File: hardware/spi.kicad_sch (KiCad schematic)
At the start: 20 parts, among them J2 Conn_LAN_Module, J3 Conn_SD_Module, J4 Conn_SD_ACT_LED, U2 DG412, U3 74LVC00, U5 74LVC32, U6 74LVC74, U7 74LVC02

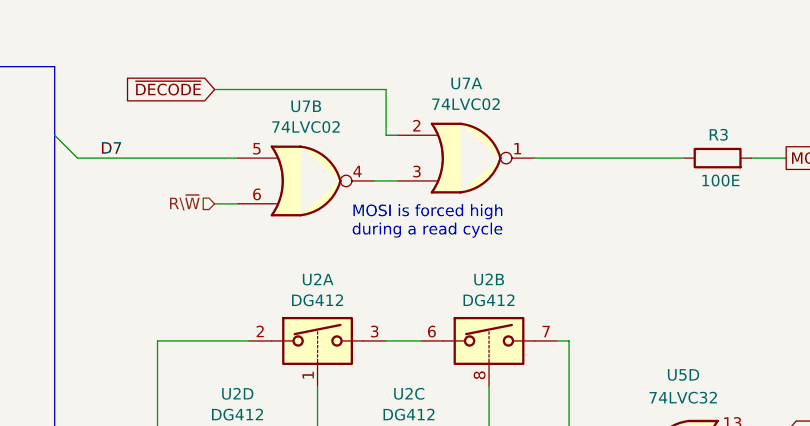
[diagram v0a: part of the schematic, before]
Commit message: Added info on MOSI setup mod to schematics
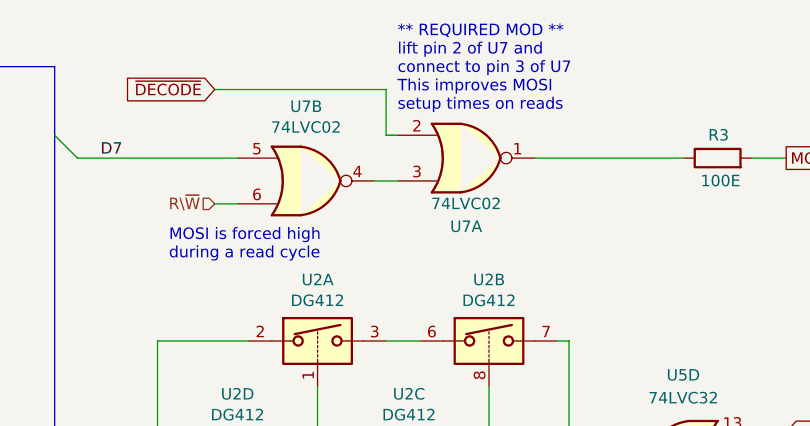
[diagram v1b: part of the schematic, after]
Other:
- note added: "** REQUIRED MOD ** lift pin 2 of U7 and connect to pin 3 of U7 This improves MOSI setup times on reads"
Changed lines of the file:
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@@
     (comment 1 "rev 1.1: new address decoder, 3V3 supplied by SD module, MOSI forced high on read")
     (comment 2 "rev 1.2: fixed small but fatal bug in address decoder, smaller PCB to clear shield")
+    (comment 3 "NOTE 5-12-2022: mod required on U7, see schematics")
   )
   (junction (at 78.74 153.67) (diameter 0) (color 0 0 0 0)
@@
     (effects (font (size 1.27 1.27)) (justify left bottom))
   )
-  (text "MOSI is forced high\nduring a read cycle" (at 168.91 36.83 0)
+  (text "MOSI is forced high\nduring a read cycle" (at 148.59 39.37 0)
     (effects (font (size 1.27 1.27)) (justify left bottom))
   )
@@
     (effects (font (size 1.27 1.27)) (justify left bottom))
   )
+  (text "** REQUIRED MOD **\nlift pin 2 of U7 and \nconnect to pin 3 of U7\nThis improves MOSI \nsetup times on reads"
+    (at 173.99 22.86 0)
+    (effects (font (size 1.27 1.27)) (justify left bottom))
+  )
   (label "D8" (at 140.97 95.25 0)
     (effects (font (size 1.27 1.27)) (justify left bottom))
@@
   (symbol (lib_id "74xx:74HC02") (at 181.61 27.94 0) (unit 1)
     (in_bom yes) (on_board yes)
-    (property "Reference" "U7" (id 0) (at 181.61 19.685 0))
-    (property "Value" "74LVC02" (id 1) (at 181.61 21.9964 0))
+    (property "Reference" "U7" (id 0) (at 181.61 35.56 0))
+    (property "Value" "74LVC02" (id 1) (at 181.61 33.02 0))
     (property "Footprint" "Package_SO:SOIC-14_3.9x8.7mm_P1.27mm" (id 2) (at 181.61 27.94 0)
       (effects (font (size 1.27 1.27)) hide)

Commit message: New Revision 1.3 which improves MOSI setup times on reads
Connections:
- net GND: now also U7.2
- net ~{DECODE}: no longer U7.2
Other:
- note removed: "** REQUIRED MOD ** lift pin 2 of U7 and connect to pin 3 of U7 This improves MOSI setup times on reads"
- moved on the sheet: R3, U7A, U7B
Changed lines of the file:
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@@
   (title_block
     (title "A500 simple SPI controller")
-    (date "2022-11-16")
-    (rev "1.2")
+    (date "2022-12-05")
+    (rev "1.3")
     (company "Dennis van Weeren")
     (comment 1 "rev 1.1: new address decoder, 3V3 supplied by SD module, MOSI forced high on read")
     (comment 2 "rev 1.2: fixed small but fatal bug in address decoder, smaller PCB to clear shield")
-    (comment 3 "NOTE 5-12-2022: mod required on U7, see schematics")
+    (comment 3 "rev 1.3: improved MOSI setup time on reads")
   )
   (junction (at 78.74 153.67) (diameter 0) (color 0 0 0 0)
@@
     (stroke (width 0) (type default) (color 0 0 0 0))
   )
-  (bus_entry (at 135.89 25.4) (size 2.54 2.54)
+  (bus_entry (at 135.89 21.59) (size 2.54 2.54)
     (stroke (width 0) (type default) (color 0 0 0 0))
   )
@@
     (stroke (width 0) (type default) (color 0 0 0 0))
   )
+  (wire (pts (xy 176.53 31.75) (xy 176.53 33.02))
+    (stroke (width 0) (type default) (color 0 0 0 0))
+  )
   (wire (pts (xy 15.24 153.67) (xy 27.94 153.67))
     (stroke (width 0) (type default) (color 0 0 0 0))
@@
     (stroke (width 0) (type default) (color 0 0 0 0))
   )
+  (wire (pts (xy 177.8 31.75) (xy 176.53 31.75))
+    (stroke (width 0) (type default) (color 0 0 0 0))
+  )
   (wire (pts (xy 214.63 63.5) (xy 214.63 64.77))
     (stroke (width 0) (type default) (color 0 0 0 0))
@@
     (stroke (width 0) (type default) (color 0 0 0 0))
   )
-  (wire (pts (xy 173.99 25.4) (xy 172.72 25.4))
-    (stroke (width 0) (type default) (color 0 0 0 0))
-  )
   (wire (pts (xy 203.2 100.33) (xy 203.2 104.14))
     (stroke (width 0) (type default) (color 0 0 0 0))
@@
     (stroke (width 0) (type default) (color 0 0 0 0))
   )
-  (wire (pts (xy 171.45 30.48) (xy 173.99 30.48))
+  (wire (pts (xy 171.45 26.67) (xy 177.8 26.67))
     (stroke (width 0) (type default) (color 0 0 0 0))
   )
@@
     (stroke (width 0) (type default) (color 0 0 0 0))
   )
-  (wire (pts (xy 138.43 27.94) (xy 156.21 27.94))
+  (wire (pts (xy 138.43 24.13) (xy 156.21 24.13))
     (stroke (width 0) (type default) (color 0 0 0 0))
   )
@@
     (stroke (width 0) (type default) (color 0 0 0 0))
   )
-  (wire (pts (xy 153.67 20.32) (xy 172.72 20.32))
-    (stroke (width 0) (type default) (color 0 0 0 0))
-  )
   (bus (pts (xy 34.29 58.42) (xy 34.29 76.2))
     (stroke (width 0) (type default) (color 0 0 0 0))
@@
     (stroke (width 0) (type default) (color 0 0 0 0))
   )
-  (wire (pts (xy 172.72 25.4) (xy 172.72 20.32))
-    (stroke (width 0) (type default) (color 0 0 0 0))
-  )
   (wire (pts (xy 15.24 152.4) (xy 15.24 153.67))
     (stroke (width 0) (type default) (color 0 0 0 0))
@@
     (stroke (width 0) (type default) (color 0 0 0 0))
   )
-  (wire (pts (xy 189.23 27.94) (xy 205.74 27.94))
+  (wire (pts (xy 193.04 29.21) (xy 205.74 29.21))
     (stroke (width 0) (type default) (color 0 0 0 0))
   )
@@
     (stroke (width 0) (type default) (color 0 0 0 0))
   )
-  (wire (pts (xy 213.36 27.94) (xy 217.17 27.94))
+  (wire (pts (xy 213.36 29.21) (xy 217.17 29.21))
     (stroke (width 0) (type default) (color 0 0 0 0))
   )
@@
     (stroke (width 0) (type default) (color 0 0 0 0))
   )
-  (bus (pts (xy 135.89 25.4) (xy 135.89 58.42))
+  (bus (pts (xy 135.89 21.59) (xy 135.89 58.42))
     (stroke (width 0) (type default) (color 0 0 0 0))
   )
@@
     (stroke (width 0) (type default) (color 0 0 0 0))
   )
-  (bus (pts (xy 135.89 17.78) (xy 135.89 25.4))
+  (bus (pts (xy 135.89 17.78) (xy 135.89 21.59))
     (stroke (width 0) (type default) (color 0 0 0 0))
   )
@@
     (stroke (width 0) (type default) (color 0 0 0 0))
   )
-  (wire (pts (xy 156.21 33.02) (xy 153.67 33.02))
+  (wire (pts (xy 156.21 29.21) (xy 153.67 29.21))
     (stroke (width 0) (type default) (color 0 0 0 0))
   )
@@
     (effects (font (size 1.27 1.27)) (justify left bottom))
   )
-  (text "MOSI is forced high\nduring a read cycle" (at 148.59 39.37 0)
+  (text "MOSI is forced high\nduring a read cycle" (at 148.59 35.56 0)
     (effects (font (size 1.27 1.27)) (justify left bottom))
   )
@@
     (effects (font (size 1.27 1.27)) (justify left bottom))
   )
-  (text "** REQUIRED MOD **\nlift pin 2 of U7 and \nconnect to pin 3 of U7\nThis improves MOSI \nsetup times on reads"
-    (at 173.99 22.86 0)
-    (effects (font (size 1.27 1.27)) (justify left bottom))
-  )
   (label "D8" (at 140.97 95.25 0)
     (effects (font (size 1.27 1.27)) (justify left bottom))
@@
     (effects (font (size 1.27 1.27)) (justify left bottom))
   )
-  (label "D7" (at 140.97 27.94 0)
+  (label "D7" (at 140.97 24.13 0)
     (effects (font (size 1.27 1.27)) (justify left bottom))
   )
@@
     )
   )
-  (global_label "~{DECODE}" (shape input) (at 153.67 20.32 180) (fields_autoplaced)
-    (effects (font (size 1.27 1.27)) (justify right))
-    (property "Intersheet References" "${INTERSHEET_REFS}" (id 0) (at 143.8183 20.2406 0)
-      (effects (font (size 1.27 1.27)) (justify right) hide)
-    )
-  )
   (global_label "~{CS1}" (shape input) (at 266.7 104.14 0) (fields_autoplaced)
     (effects (font (size 1.27 1.27)) (justify left))
@@
     )
   )
-  (global_label "MOSI" (shape output) (at 217.17 27.94 0) (fields_autoplaced)
+  (global_label "MOSI" (shape output) (at 217.17 29.21 0) (fields_autoplaced)
     (effects (font (size 1.27 1.27)) (justify left))
-    (property "Intersheet References" "${INTERSHEET_REFS}" (id 0) (at 8.89 -2.54 0)
+    (property "Intersheet References" "${INTERSHEET_REFS}" (id 0) (at 8.89 -1.27 0)
       (effects (font (size 1.27 1.27)) hide)
     )
@@
     (effects (font (size 1.27 1.27)) (justify right))
   )
-  (hierarchical_label "R\\~{W}" (shape input) (at 153.67 33.02 180)
+  (hierarchical_label "R\\~{W}" (shape input) (at 153.67 29.21 180)
     (effects (font (size 1.27 1.27)) (justify right))
   )
@@
     (effects (font (size 1.27 1.27)) (justify right))
   )
-  (symbol (lib_id "74xx:74HC02") (at 181.61 27.94 0) (unit 1)
+  (symbol (lib_id "74xx:74HC02") (at 185.42 29.21 0) (mirror x) (unit 1)
     (in_bom yes) (on_board yes)
-    (property "Reference" "U7" (id 0) (at 181.61 35.56 0))
-    (property "Value" "74LVC02" (id 1) (at 181.61 33.02 0))
-    (property "Footprint" "Package_SO:SOIC-14_3.9x8.7mm_P1.27mm" (id 2) (at 181.61 27.94 0)
+    (property "Reference" "U7" (id 0) (at 185.42 21.59 0))
+    (property "Value" "74LVC02" (id 1) (at 185.42 24.13 0))
+    (property "Footprint" "Package_SO:SOIC-14_3.9x8.7mm_P1.27mm" (id 2) (at 185.42 29.21 0)
       (effects (font (size 1.27 1.27)) hide)
     )
-    (property "Datasheet" "http://www.ti.com/lit/gpn/sn74hc02" (id 3) (at 181.61 27.94 0)
+    (property "Datasheet" "http://www.ti.com/lit/gpn/sn74hc02" (id 3) (at 185.42 29.21 0)
       (effects (font (size 1.27 1.27)) hide)
     )
@@
     (pin "7")
   )
-  (symbol (lib_id "74xx:74HC02") (at 163.83 30.48 0) (unit 2)
+  (symbol (lib_id "74xx:74HC02") (at 163.83 26.67 0) (unit 2)
     (in_bom yes) (on_board yes)
-    (property "Reference" "U7" (id 0) (at 163.83 22.225 0))
-    (property "Value" "74LVC02" (id 1) (at 163.83 24.5364 0))
-    (property "Footprint" "Package_SO:SOIC-14_3.9x8.7mm_P1.27mm" (id 2) (at 163.83 30.48 0)
+    (property "Reference" "U7" (id 0) (at 163.83 18.415 0))
+    (property "Value" "74LVC02" (id 1) (at 163.83 20.7264 0))
+    (property "Footprint" "Package_SO:SOIC-14_3.9x8.7mm_P1.27mm" (id 2) (at 163.83 26.67 0)
       (effects (font (size 1.27 1.27)) hide)
     )
-    (property "Datasheet" "http://www.ti.com/lit/gpn/sn74hc02" (id 3) (at 163.83 30.48 0)
+    (property "Datasheet" "http://www.ti.com/lit/gpn/sn74hc02" (id 3) (at 163.83 26.67 0)
       (effects (font (size 1.27 1.27)) hide)
     )
@@
     (pin "1")
   )
-  (symbol (lib_id "Device:R") (at 209.55 27.94 90) (unit 1)
+  (symbol (lib_id "Device:R") (at 209.55 29.21 90) (unit 1)
     (in_bom yes) (on_board yes)
-    (property "Reference" "R3" (id 0) (at 210.82 25.4 90)
+    (property "Reference" "R3" (id 0) (at 210.82 26.67 90)
       (effects (font (size 1.27 1.27)) (justify left))
     )
-    (property "Value" "100E" (id 1) (at 212.09 30.48 90)
+    (property "Value" "100E" (id 1) (at 212.09 31.75 90)
       (effects (font (size 1.27 1.27)) (justify left))
     )
-    (property "Footprint" "Resistor_SMD:R_0805_2012Metric_Pad1.20x1.40mm_HandSolder" (id 2) (at 209.55 29.718 90)
+    (property "Footprint" "Resistor_SMD:R_0805_2012Metric_Pad1.20x1.40mm_HandSolder" (id 2) (at 209.55 30.988 90)
       (effects (font (size 1.27 1.27)) hide)
     )
-    (property "Datasheet" "~" (id 3) (at 209.55 27.94 0)
+    (property "Datasheet" "~" (id 3) (at 209.55 29.21 0)
       (effects (font (size 1.27 1.27)) hide)
     )
@@
       (effects (font (size 1.27 1.27)) hide)
     )
+    (pin "1")
+  )
+  (symbol (lib_id "power:GND") (at 176.53 33.02 0) (unit 1)
+    (in_bom yes) (on_board yes)
+    (property "Reference" "#PWR?" (id 0) (at 176.53 39.37 0)
+      (effects (font (size 1.27 1.27)) hide)
+    )
+    (property "Value" "GND" (id 1) (at 176.657 37.4142 0))
+    (property "Footprint" "" (id 2) (at 176.53 33.02 0)
+      (effects (font (size 1.27 1.27)) hide)
+    )
+    (property "Datasheet" "" (id 3) (at 176.53 33.02 0)
+      (effects (font (size 1.27 1.27)) hide)
+    )
